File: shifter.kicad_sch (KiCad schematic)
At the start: 11 parts

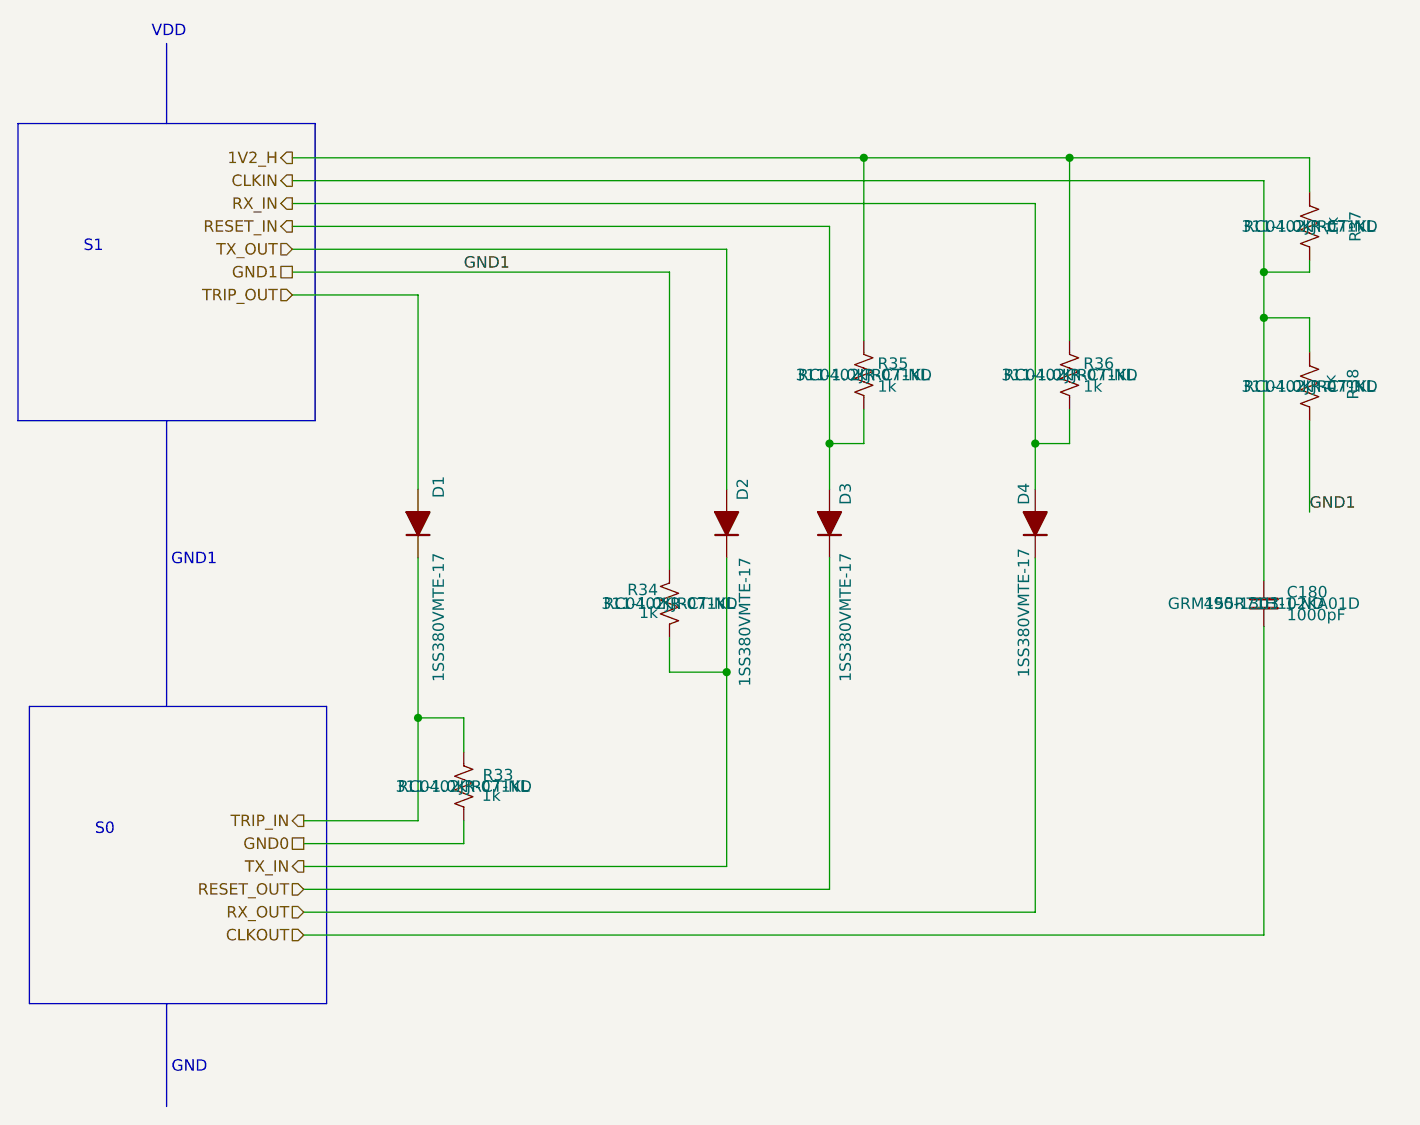
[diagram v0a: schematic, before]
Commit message: finished adding ASICs to schematic. Change VR to single phase 2.8V output
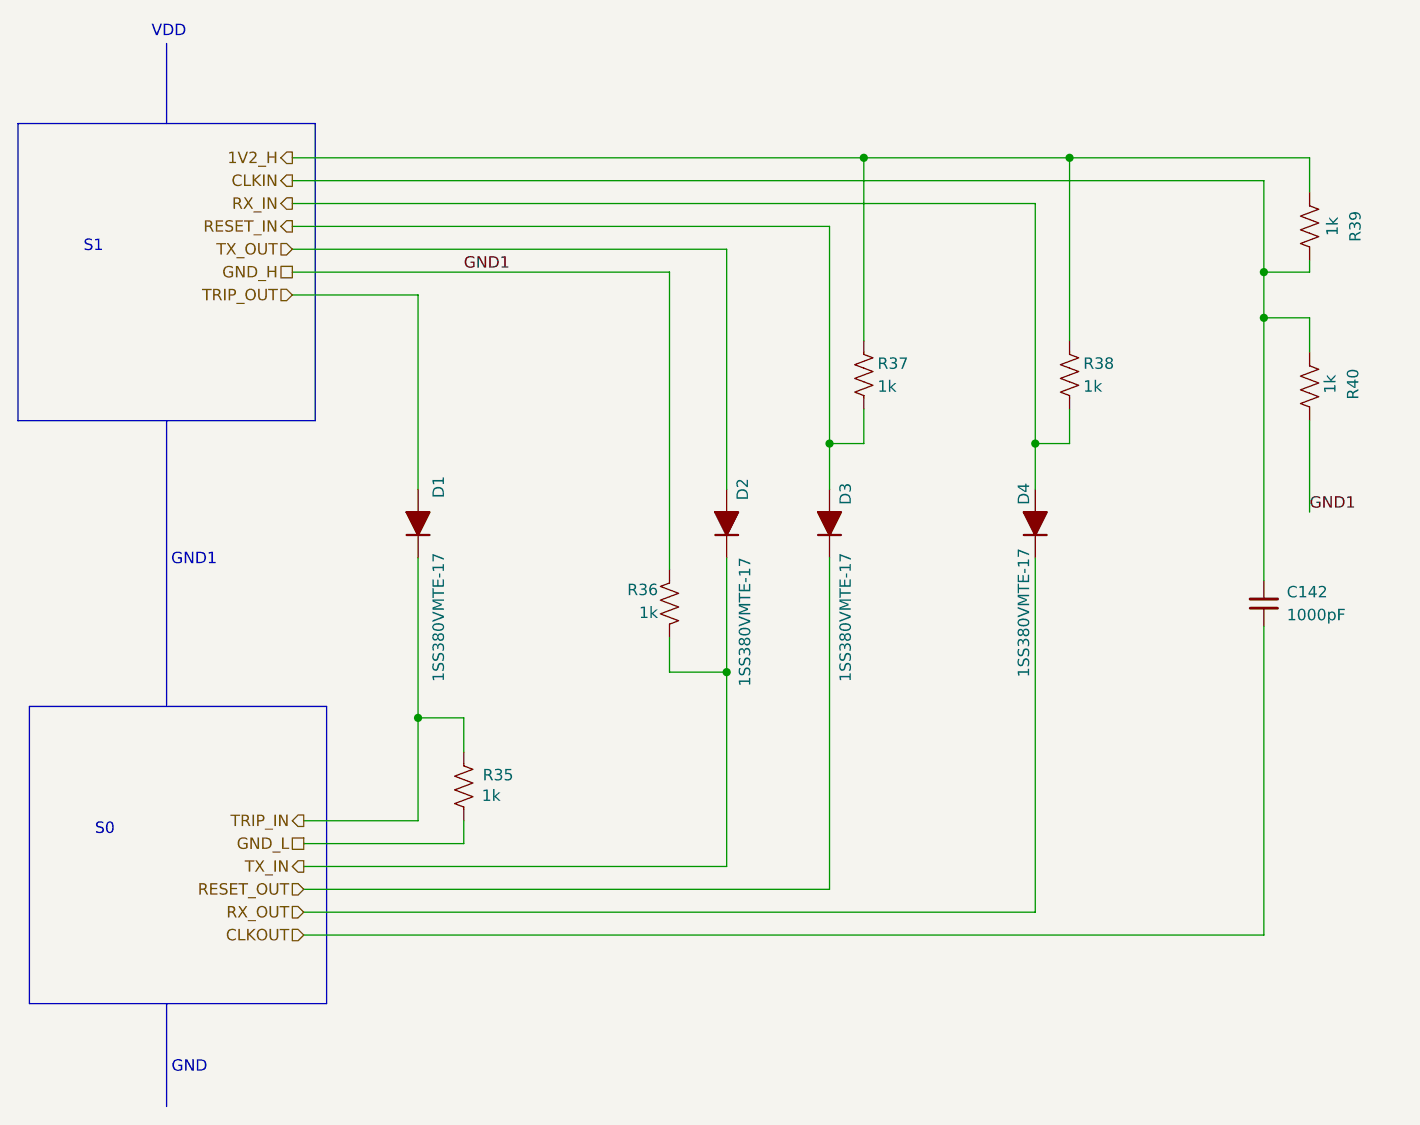
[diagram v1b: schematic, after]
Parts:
- renumbered C180 to C142, R33 to R35, R34 to R36, R35 to R37, R36 to R38, R37 to R39, R38 to R40
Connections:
- net GND0 renamed GND_L
- net GND1 renamed GND_H
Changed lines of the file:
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@@
 		)
 	)
-	(hierarchical_label "GND1"
+	(hierarchical_label "GND_H"
 		(shape passive)
 		(at 80.01 55.88 180)
@@
 		)
 	)
-	(hierarchical_label "GND0"
+	(hierarchical_label "GND_L"
 		(shape passive)
 		(at 81.28 119.38 180)
@@
 		(on_board yes)
 		(dnp no)
-		(property "Reference" "R33"
+		(property "Reference" "R35"
 			(at 102.87 111.76 0)
 			(effects
@@
 					(size 1.27 1.27)
 				)
+				(hide yes)
 			)
 		)
@@
 					(size 1.27 1.27)
 				)
+				(hide yes)
 			)
 		)
@@
 			(project "bitaxeBIRDS"
 				(path "/61fe8d2c-9301-4ad9-8caf-c47acfa835b0/5053a6d5-ae8d-4ae0-9f6e-0d65e80da719/77e107fa-f35d-45bb-bf6d-758e10cfffbd"
-					(reference "R33")
+					(reference "R35")
 					(unit 1)
 				)
 				(path "/61fe8d2c-9301-4ad9-8caf-c47acfa835b0/5053a6d5-ae8d-4ae0-9f6e-0d65e80da719/7d89e220-d1ae-4c07-8d25-5bbe4d704970"
-					(reference "R33")
+					(reference "R47")
 					(unit 1)
 				)
 				(path "/61fe8d2c-9301-4ad9-8caf-c47acfa835b0/5053a6d5-ae8d-4ae0-9f6e-0d65e80da719/8201832f-9551-4969-84e2-32187e0075ba"
-					(reference "R33")
+					(reference "R41")
 					(unit 1)
 				)
@@
 				)
 				(path "/61fe8d2c-9301-4ad9-8caf-c47acfa835b0/5053a6d5-ae8d-4ae0-9f6e-0d65e80da719/7d89e220-d1ae-4c07-8d25-5bbe4d704970"
-					(reference "D4")
+					(reference "D12")
 					(unit 1)
 				)
 				(path "/61fe8d2c-9301-4ad9-8caf-c47acfa835b0/5053a6d5-ae8d-4ae0-9f6e-0d65e80da719/8201832f-9551-4969-84e2-32187e0075ba"
-					(reference "D4")
+					(reference "D8")
 					(unit 1)
 				)
@@
 		(dnp no)
 		(fields_autoplaced yes)
-		(property "Reference" "C180"
+		(property "Reference" "C142"
 			(at 190.5 91.4335 0)
 			(effects
@@
 					(size 1.27 1.27)
 				)
+				(hide yes)
 			)
 		)
@@
 					(size 1.27 1.27)
 				)
+				(hide yes)
 			)
 		)
@@
 			(project "bitaxeBIRDS"
 				(path "/61fe8d2c-9301-4ad9-8caf-c47acfa835b0/5053a6d5-ae8d-4ae0-9f6e-0d65e80da719/77e107fa-f35d-45bb-bf6d-758e10cfffbd"
-					(reference "C180")
+					(reference "C142")
 					(unit 1)
 				)
 				(path "/61fe8d2c-9301-4ad9-8caf-c47acfa835b0/5053a6d5-ae8d-4ae0-9f6e-0d65e80da719/7d89e220-d1ae-4c07-8d25-5bbe4d704970"
-					(reference "C180")
+					(reference "C144")
 					(unit 1)
 				)
 				(path "/61fe8d2c-9301-4ad9-8caf-c47acfa835b0/5053a6d5-ae8d-4ae0-9f6e-0d65e80da719/8201832f-9551-4969-84e2-32187e0075ba"
-					(reference "C180")
+					(reference "C143")
 					(unit 1)
 				)
@@
 		(on_board yes)
 		(dnp no)
-		(property "Reference" "R38"
+		(property "Reference" "R40"
 			(at 197.866 68.326 90)
 			(effects
@@
 					(size 1.27 1.27)
 				)
+				(hide yes)
 			)
 		)
@@
 					(size 1.27 1.27)
 				)
+				(hide yes)
 			)
 		)
@@
 			(project "bitaxeBIRDS"
 				(path "/61fe8d2c-9301-4ad9-8caf-c47acfa835b0/5053a6d5-ae8d-4ae0-9f6e-0d65e80da719/77e107fa-f35d-45bb-bf6d-758e10cfffbd"
-					(reference "R38")
+					(reference "R40")
 					(unit 1)
 				)
 				(path "/61fe8d2c-9301-4ad9-8caf-c47acfa835b0/5053a6d5-ae8d-4ae0-9f6e-0d65e80da719/7d89e220-d1ae-4c07-8d25-5bbe4d704970"
-					(reference "R38")
+					(reference "R52")
 					(unit 1)
 				)
 				(path "/61fe8d2c-9301-4ad9-8caf-c47acfa835b0/5053a6d5-ae8d-4ae0-9f6e-0d65e80da719/8201832f-9551-4969-84e2-32187e0075ba"
-					(reference "R38")
+					(reference "R46")
 					(unit 1)
 				)
@@
 				)
 				(path "/61fe8d2c-9301-4ad9-8caf-c47acfa835b0/5053a6d5-ae8d-4ae0-9f6e-0d65e80da719/7d89e220-d1ae-4c07-8d25-5bbe4d704970"
-					(reference "D1")
+					(reference "D9")
 					(unit 1)
 				)
 				(path "/61fe8d2c-9301-4ad9-8caf-c47acfa835b0/5053a6d5-ae8d-4ae0-9f6e-0d65e80da719/8201832f-9551-4969-84e2-32187e0075ba"
-					(reference "D1")
+					(reference "D5")
 					(unit 1)
 				)
@@
 		(on_board yes)
 		(dnp no)
-		(property "Reference" "R34"
+		(property "Reference" "R36"
 			(at 120.65 91.186 0)
 			(effects
@@
 					(size 1.27 1.27)
 				)
+				(hide yes)
 			)
 		)
@@
 					(size 1.27 1.27)
 				)
+				(hide yes)
 			)
 		)
@@
 			(project "bitaxeBIRDS"
 				(path "/61fe8d2c-9301-4ad9-8caf-c47acfa835b0/5053a6d5-ae8d-4ae0-9f6e-0d65e80da719/77e107fa-f35d-45bb-bf6d-758e10cfffbd"
-					(reference "R34")
+					(reference "R36")
 					(unit 1)
 				)
 				(path "/61fe8d2c-9301-4ad9-8caf-c47acfa835b0/5053a6d5-ae8d-4ae0-9f6e-0d65e80da719/7d89e220-d1ae-4c07-8d25-5bbe4d704970"
-					(reference "R34")
+					(reference "R48")
 					(unit 1)
 				)
 				(path "/61fe8d2c-9301-4ad9-8caf-c47acfa835b0/5053a6d5-ae8d-4ae0-9f6e-0d65e80da719/8201832f-9551-4969-84e2-32187e0075ba"
-					(reference "R34")
+					(reference "R42")
 					(unit 1)
 				)
@@
 				)
 				(path "/61fe8d2c-9301-4ad9-8caf-c47acfa835b0/5053a6d5-ae8d-4ae0-9f6e-0d65e80da719/7d89e220-d1ae-4c07-8d25-5bbe4d704970"
-					(reference "D3")
+					(reference "D11")
 					(unit 1)
 				)
 				(path "/61fe8d2c-9301-4ad9-8caf-c47acfa835b0/5053a6d5-ae8d-4ae0-9f6e-0d65e80da719/8201832f-9551-4969-84e2-32187e0075ba"
-					(reference "D3")
+					(reference "D7")
 					(unit 1)
 				)
@@
 		(on_board yes)
 		(dnp no)
-		(property "Reference" "R35"
+		(property "Reference" "R37"
 			(at 145.034 66.04 0)
 			(effects
@@
 					(size 1.27 1.27)
 				)
+				(hide yes)
 			)
 		)
@@
 					(size 1.27 1.27)
 				)
+				(hide yes)
 			)
 		)
@@
 			(project "bitaxeBIRDS"
 				(path "/61fe8d2c-9301-4ad9-8caf-c47acfa835b0/5053a6d5-ae8d-4ae0-9f6e-0d65e80da719/77e107fa-f35d-45bb-bf6d-758e10cfffbd"
-					(reference "R35")
+					(reference "R37")
 					(unit 1)
 				)
 				(path "/61fe8d2c-9301-4ad9-8caf-c47acfa835b0/5053a6d5-ae8d-4ae0-9f6e-0d65e80da719/7d89e220-d1ae-4c07-8d25-5bbe4d704970"
-					(reference "R35")
+					(reference "R49")
 					(unit 1)
 				)
 				(path "/61fe8d2c-9301-4ad9-8caf-c47acfa835b0/5053a6d5-ae8d-4ae0-9f6e-0d65e80da719/8201832f-9551-4969-84e2-32187e0075ba"
-					(reference "R35")
+					(reference "R43")
 					(unit 1)
 				)
@@
 				)
 				(path "/61fe8d2c-9301-4ad9-8caf-c47acfa835b0/5053a6d5-ae8d-4ae0-9f6e-0d65e80da719/7d89e220-d1ae-4c07-8d25-5bbe4d704970"
-					(reference "D2")
+					(reference "D10")
 					(unit 1)
 				)
 				(path "/61fe8d2c-9301-4ad9-8caf-c47acfa835b0/5053a6d5-ae8d-4ae0-9f6e-0d65e80da719/8201832f-9551-4969-84e2-32187e0075ba"
-					(reference "D2")
+					(reference "D6")
 					(unit 1)
 				)
@@
 		(on_board yes)
 		(dnp no)
-		(property "Reference" "R36"
+		(property "Reference" "R38"
 			(at 167.894 66.04 0)
 			(effects
@@
 					(size 1.27 1.27)
 				)
+				(hide yes)
 			)
 		)
@@
 					(size 1.27 1.27)
 				)
+				(hide yes)
 			)
 		)
@@
 			(project "bitaxeBIRDS"
 				(path "/61fe8d2c-9301-4ad9-8caf-c47acfa835b0/5053a6d5-ae8d-4ae0-9f6e-0d65e80da719/77e107fa-f35d-45bb-bf6d-758e10cfffbd"
-					(reference "R36")
+					(reference "R38")
 					(unit 1)
 				)
 				(path "/61fe8d2c-9301-4ad9-8caf-c47acfa835b0/5053a6d5-ae8d-4ae0-9f6e-0d65e80da719/7d89e220-d1ae-4c07-8d25-5bbe4d704970"
-					(reference "R36")
+					(reference "R50")
 					(unit 1)
 				)
 				(path "/61fe8d2c-9301-4ad9-8caf-c47acfa835b0/5053a6d5-ae8d-4ae0-9f6e-0d65e80da719/8201832f-9551-4969-84e2-32187e0075ba"
-					(reference "R36")
+					(reference "R44")
 					(unit 1)
 				)
@@
 		(on_board yes)
 		(dnp no)
-		(property "Reference" "R37"
+		(property "Reference" "R39"
 			(at 198.12 50.8 90)
 			(effects
@@
 					(size 1.27 1.27)
 				)
+				(hide yes)
 			)
 		)
@@
 					(size 1.27 1.27)
 				)
+				(hide yes)
 			)
 		)
@@
 			(project "bitaxeBIRDS"
 				(path "/61fe8d2c-9301-4ad9-8caf-c47acfa835b0/5053a6d5-ae8d-4ae0-9f6e-0d65e80da719/77e107fa-f35d-45bb-bf6d-758e10cfffbd"
-					(reference "R37")
+					(reference "R39")
 					(unit 1)
 				)
 				(path "/61fe8d2c-9301-4ad9-8caf-c47acfa835b0/5053a6d5-ae8d-4ae0-9f6e-0d65e80da719/7d89e220-d1ae-4c07-8d25-5bbe4d704970"
-					(reference "R37")
+					(reference "R51")
 					(unit 1)
 				)
 				(path "/61fe8d2c-9301-4ad9-8caf-c47acfa835b0/5053a6d5-ae8d-4ae0-9f6e-0d65e80da719/8201832f-9551-4969-84e2-32187e0075ba"
-					(reference "R37")
-					(unit 1)
-				)
+					(reference "R45")
+					(unit 1)
+				)

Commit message: switched to smaller level shifter diodes. switched ASIC modes
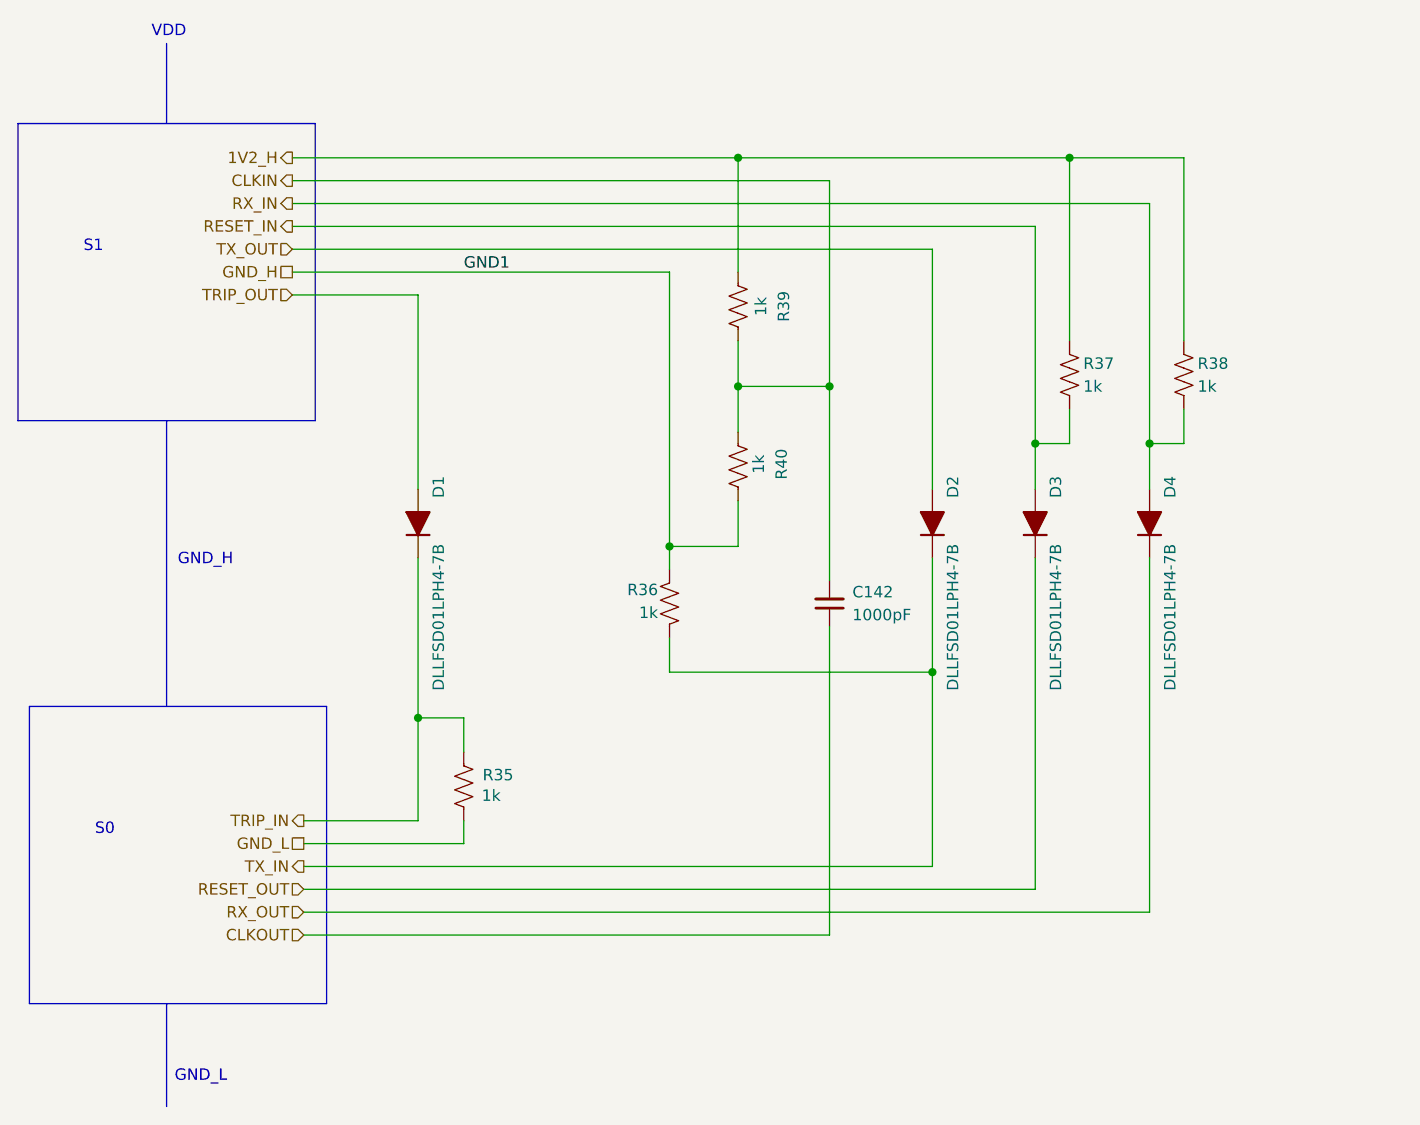
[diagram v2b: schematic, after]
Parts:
- D1, D2, D3, D4: value 1SS380VMTE-17 -> DLLFSD01LPH4-7B; footprint bitaxe:SOD-323FLUMD2_ROM -> bitaxe:DIODE_DLLFSD01LPH4-7B_DIO; DK 846-1SS380VMTE-17CT-ND -> 31-DLLFSD01LPH4-7BCT-ND; PARTNO 1SS380VMTE-17 -> DLLFSD01LPH4-7B
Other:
- note added: "GND_H"
- note added: "GND_L"
- note removed: "GND"
- note removed: "GND1"
- moved on the sheet: C142, D2, D3, D4, R37, R38, R39, R40

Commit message: unify 1k resistor part numbers
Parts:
- R35, R36, R37, R38, R39, R40: DK 311-1.0KJRCT-ND -> 311-1.00KLRCT-ND; PARTNO RC0402JR-071KL -> RC0402FR-071KL
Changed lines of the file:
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@@
 			)
 		)
-		(property "DK" "311-1.0KJRCT-ND"
+		(property "DK" "311-1.00KLRCT-ND"
 			(at 99.06 113.03 0)
 			(effects
@@
 			)
 		)
-		(property "PARTNO" "RC0402JR-071KL"
+		(property "PARTNO" "RC0402FR-071KL"
 			(at 99.06 113.03 0)
 			(effects
@@
 			)
 		)
-		(property "DK" "311-1.0KJRCT-ND"
+		(property "DK" "311-1.00KLRCT-ND"
 			(at 129.54 77.47 0)
 			(effects
@@
 			)
 		)
-		(property "PARTNO" "RC0402JR-071KL"
+		(property "PARTNO" "RC0402FR-071KL"
 			(at 129.54 77.47 0)
 			(effects
@@
 			)
 		)
-		(property "DK" "311-1.0KJRCT-ND"
+		(property "DK" "311-1.00KLRCT-ND"
 			(at 121.92 92.71 0)
 			(effects
@@
 			)
 		)
-		(property "PARTNO" "RC0402JR-071KL"
+		(property "PARTNO" "RC0402FR-071KL"
 			(at 121.92 92.71 0)
 			(effects
@@
 			)
 		)
-		(property "DK" "311-1.0KJRCT-ND"
+		(property "DK" "311-1.00KLRCT-ND"
 			(at 166.37 67.31 0)
 			(effects
@@
 			)
 		)
-		(property "PARTNO" "RC0402JR-071KL"
+		(property "PARTNO" "RC0402FR-071KL"
 			(at 166.37 67.31 0)
 			(effects
@@
 			)
 		)
-		(property "DK" "311-1.0KJRCT-ND"
+		(property "DK" "311-1.00KLRCT-ND"
 			(at 179.07 67.31 0)
 			(effects
@@
 			)
 		)
-		(property "PARTNO" "RC0402JR-071KL"
+		(property "PARTNO" "RC0402FR-071KL"
 			(at 179.07 67.31 0)
 			(effects
@@
 			)
 		)
-		(property "DK" "311-1.0KJRCT-ND"
+		(property "DK" "311-1.00KLRCT-ND"
 			(at 129.54 59.69 0)
 			(effects
@@
 			)
 		)
-		(property "PARTNO" "RC0402JR-071KL"
+		(property "PARTNO" "RC0402FR-071KL"
 			(at 129.54 59.69 0)
 			(effects
